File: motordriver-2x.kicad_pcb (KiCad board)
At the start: 4 copper layers, 641 parts, among them J1 USB_B_Micro, J2 CONN_RJ45_MAG, J3 CONN_RJ45_MAG, P1 CONN_BUTTON, P11 CONN_JOYSTICK, P13 CONN_SENSOR, P14 CONN_SENSOR, P15 CONN_SENSOR, P16 CONN_SENSOR, P17 CONN_DEBUG_2R, P18 CONN_POWER_41A, P19 CONN_CAN, P2 CONN_BUTTON, P20 CONN_CAN, P21 CONN_AN_OUT, P22 CONN_AN_OUT, P23 CONN_POWER_10A, P24 CONN_CAN, P25 CONN_LCD, P26 CONN_AN_OUT, P27 CONN_AN_OUT, P28 CONN_UEXT, P3 CONN_BUTTON, P37 ENCODER, P38 CONN_SENSOR, P39 CONN_SENSOR, P4 CONN_BUTTON, P40 CONN_SENSOR, P41 ENCODER, P42 CONN_SENSOR, P43 CONN_SENSOR, P44 CONN_SENSOR, P45 CONN_MOTOR, P46 CONN_MOTOR, P47 CONN_HALL, P48 CONN_HALL, P49 CONN_BRKRES, P5 CONN_BUTTON, P6 CONN_BUTTON, P7 CONN_BUTTON, P8 CONN_BUTTON, P9 CONN_JOYSTICK, Q1 Q_NMOS_2X_60V_63A, Q2 Q_NMOS_2X_60V_63A, Q3 Q_NMOS_2X_60V_63A, Q4 Q_NMOS_2X_60V_63A, Q5 Q_NMOS_2X_60V_63A, Q6 Q_NMOS_2X_60V_63A, Q7 Q_PNP_BC856, Q8 Q_NMOS_BUK9875, U1 IC_MIC2026, U10 IC_MCP4461, U11 IC_MCP2517FD-xJHA, U12 IC_STM32F429ZET6, U13 IC_MCP23S17, U14 IC_TPS54360DDA, U15 IC_TJA1044GT3, U16 IC_TLV2474, U17 IC_M24C16, U18 IC_USBLC6-2, U19 IC_TPS62147RGXR, U2 IC_MAX6818, U20 IC_TLV75533, U21 IC_LP55231, U22 IC_TLV75533, U23 IC_MAX14890, U24 IC_MAX14890, U25 IC_MIC2026, U26 IC_TLV2474, U27 IC_USBLC6-2, U28 IC_USBLC6-2, U29 IC_MCP4461, U3 IC_TLV2474, U30 IC_LAN9252, U31 IC_DRV8302, U32 IC_DRV8302, U33 IC_TLV2474, U34 IC_M24C16, U35 IC_TLV2474, U36 IC_TLV75533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

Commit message: power supply layout
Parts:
- added C51: CAP_2.2uF_16V_0402, Capacitor_SMD:C_0402_1005Metric, F.Cu at (377.4, -101.4)
- P37, P41: value ENCODER -> CONN_ENCODER
- moved U19 374.3 mm to (383.8, -120.2), turned to 90 degrees
- moved C55 359.3 mm to (389.0, -123.0), turned to 90 degrees
- moved C38 353.6 mm to (353.2, -114.0), turned to 180 degrees
- moved D16 351.6 mm to (387.0, -107.0), turned to 270 degrees
- moved C15 337.5 mm to (365.6, -120.2), turned to 90 degrees
- moved TP21 337.4 mm to (393.2, -117.4), turned to 90 degrees
- moved D9 335.2 mm to (350.6, -122.6), turned to 270 degrees
- moved R55 333.9 mm to (374.8, -112.0), turned to 90 degrees
- moved D28 333.7 mm to (356.6, -122.6), turned to 90 degrees
- moved D12 331.7 mm to (353.0, -107.0), turned to 180 degrees
- moved U22 331.1 mm to (380.4, -108.2)
- moved D30 326.1 mm to (387.0, -99.4), turned to 270 degrees
- moved R76 324.3 mm to (391.2, -101.6), turned to 180 degrees
- moved R58 317.3 mm to (387.4, -120.4)
- moved R62 316.7 mm to (377.4, -108.0)
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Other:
- board outline added: 200 x 127.2 mm
- board text added: "POWER"

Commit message: cpu layout
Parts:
- C28, C29, C34, C35, C39, C41, C42, C43, C44, C47, C48, C6: moved to B.Cu
- moved P20 228.2 mm to (323.0, 102.7), turned to 90 degrees
- moved U11 221.5 mm to (314.9, 107.3), turned to 90 degrees
- moved D10 214.8 mm to (318.0, 86.6)
- moved P19 211.7 mm to (323.0, 90.5), turned to 90 degrees
- moved D13 208.5 mm to (318.0, 100.6)
- moved P24 207.1 mm to (323.0, 114.8), turned to 90 degrees
- moved C42 200.6 mm to (38.2, 165.6)
- moved Y2 185.5 mm to (315.3, 112.9), turned to 270 degrees
- moved C43 184.7 mm to (48.6, 154.8), turned to 270 degrees
- moved C6 184.7 mm to (38.2, 171.2)
- moved C47 184.1 mm to (43.2, 154.8), turned to 270 degrees
- moved C44 176.5 mm to (38.2, 160.2)
- moved R198 176.0 mm to (51.4, 190.0)
- moved D31 175.0 mm to (54.0, 190.2)
- moved S1 168.6 mm to (66.4, 158.0)
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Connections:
- P19 pad 1: Net-(D10-Pad1) -> Net-(D10-Pad2)
- P19 pad 2: Net-(D10-Pad2) -> Net-(D10-Pad1)
- P20 pad 1: Net-(D11-Pad1) -> Net-(D11-Pad2)
- P20 pad 2: Net-(D11-Pad2) -> Net-(D11-Pad1)
- P24 pad 1: Net-(D13-Pad1) -> Net-(D13-Pad2)
- P24 pad 2: Net-(D13-Pad2) -> Net-(D13-Pad1)
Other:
- board text added: "CAN"

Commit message: save latest schematic
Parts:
- C111, C93: moved to F.Cu
- C40: moved to B.Cu
- moved R197 576.0 mm to (232.6, -414.4), turned to 270 degrees
- moved D29 574.1 mm to (223.2, -421.2)
- moved R196 572.5 mm to (241.6, -406.2), turned to 270 degrees
- moved TP61 570.8 mm to (165.2, -423.6)
- moved R43 570.0 mm to (209.0, -422.8), turned to 180 degrees
- moved Q7 569.5 mm to (239.2, -405.8)
- moved TP41 568.7 mm to (228.5, -405.2), turned to 180 degrees
- moved TP62 564.4 mm to (165.2, -424.6)
- moved Q8 563.6 mm to (237.8, -412.6)
- moved TP16 562.9 mm to (168.0, -446.1), turned to 180 degrees
- moved TP17 558.7 mm to (168.0, -445.2), turned to 180 degrees
- moved D27 554.3 mm to (235.0, -406.4)
- moved R195 551.8 mm to (233.0, -404.8), turned to 180 degrees
- moved TP55 540.1 mm to (228.5, -404.0), turned to 180 degrees
- moved TP81 532.7 mm to (12.1, -338.9)
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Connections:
- TP39 pad 1: Net-(R80-Pad2) -> Net-(R81-Pad2)
- TP40 pad 1: Net-(R82-Pad2) -> Net-(R83-Pad2)
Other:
- board size 200 x 127.2 mm -> 200 x 127.4 mm

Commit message: come up with pcb outline
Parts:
- added MT1: MOUNT_HOLE, MountingHole:MountingHole_3.2mm_M3_Pad, F.Cu at (255.7, 28.5)
- added MT2: MOUNT_HOLE, MountingHole:MountingHole_3.2mm_M3_Pad, F.Cu at (50.4, 148.7)
- added MT3: MOUNT_HOLE, MountingHole:MountingHole_3.2mm_M3_Pad, F.Cu at (255.0, 149.5)
- added MT4: MOUNT_HOLE, MountingHole:MountingHole_3.2mm_M3_Pad, F.Cu at (50.2, 29.0)
- C156, C157: moved to B.Cu
- moved R40 572.9 mm to (96.4, 100.9), turned to 0 degrees
- moved R49 572.3 mm to (104.0, 102.2), turned to 0 degrees
- moved R48 570.3 mm to (104.0, 101.2), turned to 180 degrees
- moved C166 568.4 mm to (104.0, 100.2), turned to 0 degrees
- moved C19 566.4 mm to (104.0, 99.2), turned to 0 degrees
- moved U14 565.2 mm to (99.0, 97.6), turned to 0 degrees
- moved R38 564.4 mm to (104.0, 98.2), turned to 0 degrees
- moved P23 563.0 mm to (113.2, 101.0), turned to 270 degrees
- moved C167 562.8 mm to (93.2, 92.7), turned to 0 degrees
- moved R37 562.5 mm to (104.0, 97.2), turned to 180 degrees
- moved D30 560.7 mm to (131.7, 101.9), turned to 270 degrees
- moved C18 560.5 mm to (104.0, 96.2), turned to 0 degrees
- moved R67 560.5 mm to (122.1, 100.9), turned to 0 degrees
- moved C165 560.1 mm to (93.2, 89.1), turned to 0 degrees
- moved U36 559.5 mm to (125.1, 100.7), turned to 0 degrees
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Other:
- board size 200 x 127.4 mm -> 215 x 130.1 mm
- board text removed: "MOTOR 2"
- board text removed: "POWER"
- board text removed: "Supply Sense"

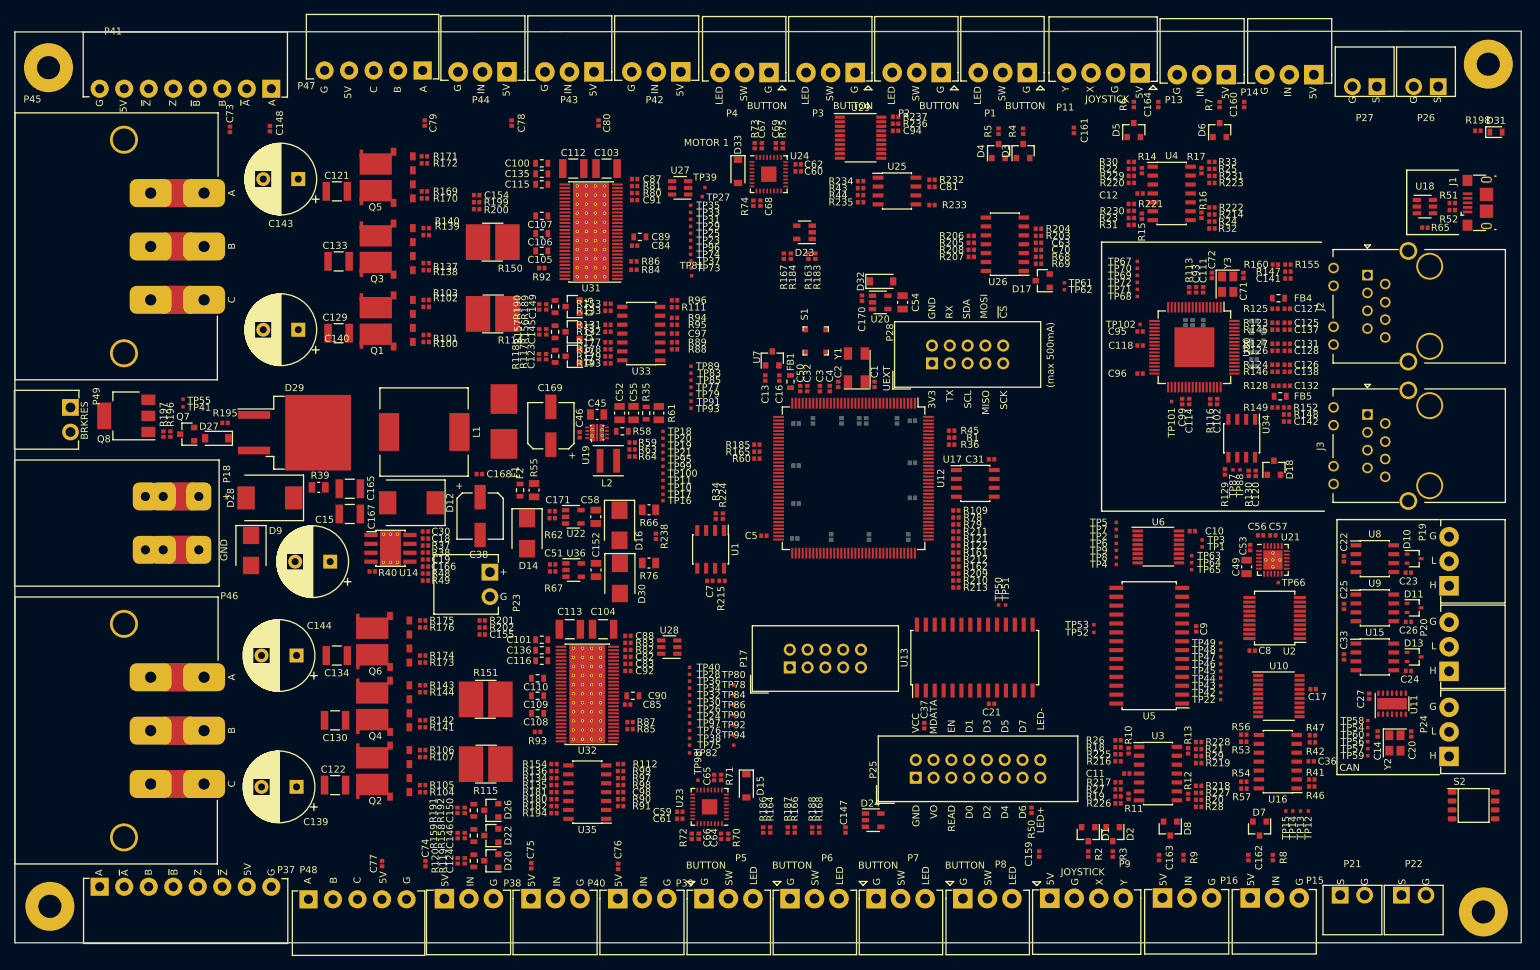
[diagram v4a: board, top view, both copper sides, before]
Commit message: better placement
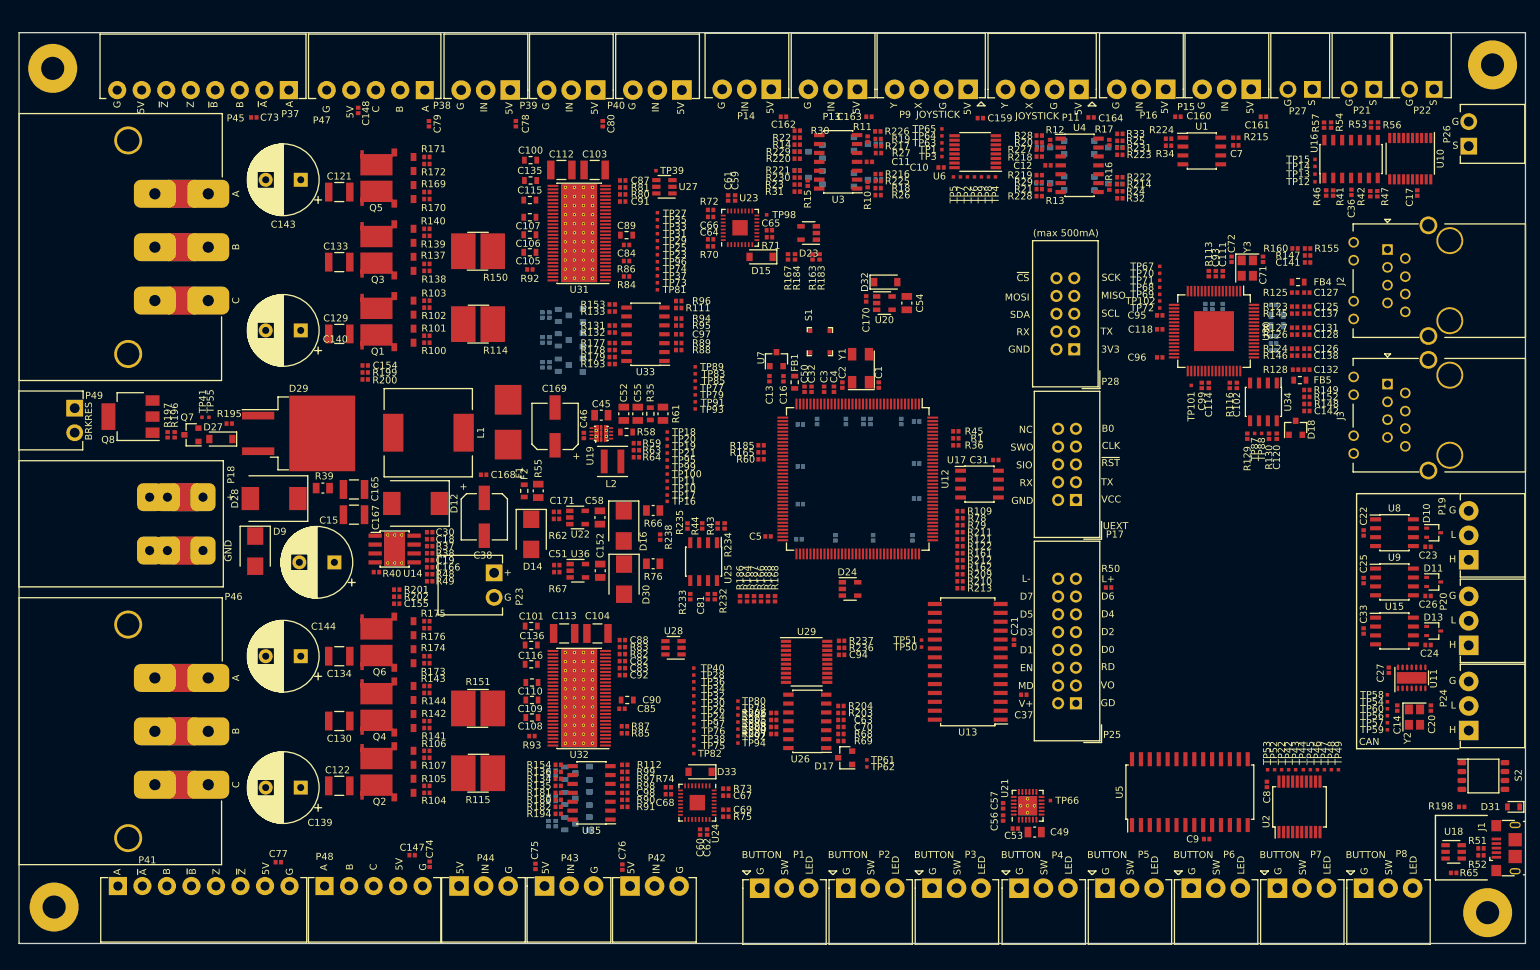
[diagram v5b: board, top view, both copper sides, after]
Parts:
- C123, C124, C145, C146, C149, C150, D1, D19, D2, D20, D21, D22, D25, D26, D3, D4, D5, D6, D7, D8, R117, R118, R119, R120, R156, R157, R158, R159, R189, R190, R191, R192, R2, R3, R4, R5, R6, R7, R8, R9: moved to B.Cu
- moved C162 124.8 mm to (155.1, 36.0), turned to 0 degrees
- moved P1 122.5 mm to (151.7, 146.1), turned to 0 degrees
- moved P4 121.7 mm to (188.7, 146.1), turned to 0 degrees
- moved P40 117.4 mm to (140.6, 32.2), turned to 180 degrees
- moved P2 117.2 mm to (164.0, 146.1), turned to 0 degrees
- moved P3 116.9 mm to (176.3, 146.1), turned to 0 degrees
- moved P37 116.9 mm to (84.5, 32.2), turned to 180 degrees
- moved P42 116.4 mm to (133.2, 145.8), turned to 0 degrees
- moved P43 116.4 mm to (121.0, 145.8), turned to 0 degrees
- moved P44 116.4 mm to (108.8, 145.8), turned to 0 degrees
- moved P9 116.0 mm to (181.5, 32.1), turned to 180 degrees
- moved P41 115.9 mm to (60.1, 145.8), turned to 0 degrees
- moved P38 115.8 mm to (116.1, 32.2), turned to 180 degrees
- moved P39 115.4 mm to (128.3, 32.2), turned to 180 degrees
- moved P16 115.4 mm to (209.7, 32.1), turned to 180 degrees
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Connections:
- U12 pad 69: ENCPWEN2 -> ENCPWEN1
- U12 pad 70: ENCPWEN1 -> ENCPWEN2
- U3 pad 10: Net-(D3-Pad3) -> Net-(D5-Pad3)
- U3 pad 12: Net-(D4-Pad3) -> Net-(D6-Pad3)
- U3 pad 13: Net-(R13-Pad2) -> Net-(R15-Pad2)
- U3 pad 14: Net-(R13-Pad1) -> Net-(R15-Pad1)
- U3 pad 8: Net-(R12-Pad1) -> Net-(R14-Pad1)
- U3 pad 9: Net-(R12-Pad2) -> Net-(R14-Pad2)
- U4 pad 1: Net-(R14-Pad1) -> Net-(R12-Pad1)
- U4 pad 2: Net-(R14-Pad2) -> Net-(R12-Pad2)
- U4 pad 3: Net-(D5-Pad3) -> Net-(D3-Pad3)
- U4 pad 5: Net-(D6-Pad3) -> Net-(D4-Pad3)
- U4 pad 6: Net-(R15-Pad2) -> Net-(R13-Pad2)
- U4 pad 7: Net-(R15-Pad1) -> Net-(R13-Pad1)
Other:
- board size 215 x 130.1 mm -> 215 x 130 mm
- board text removed: "MOTOR 1"

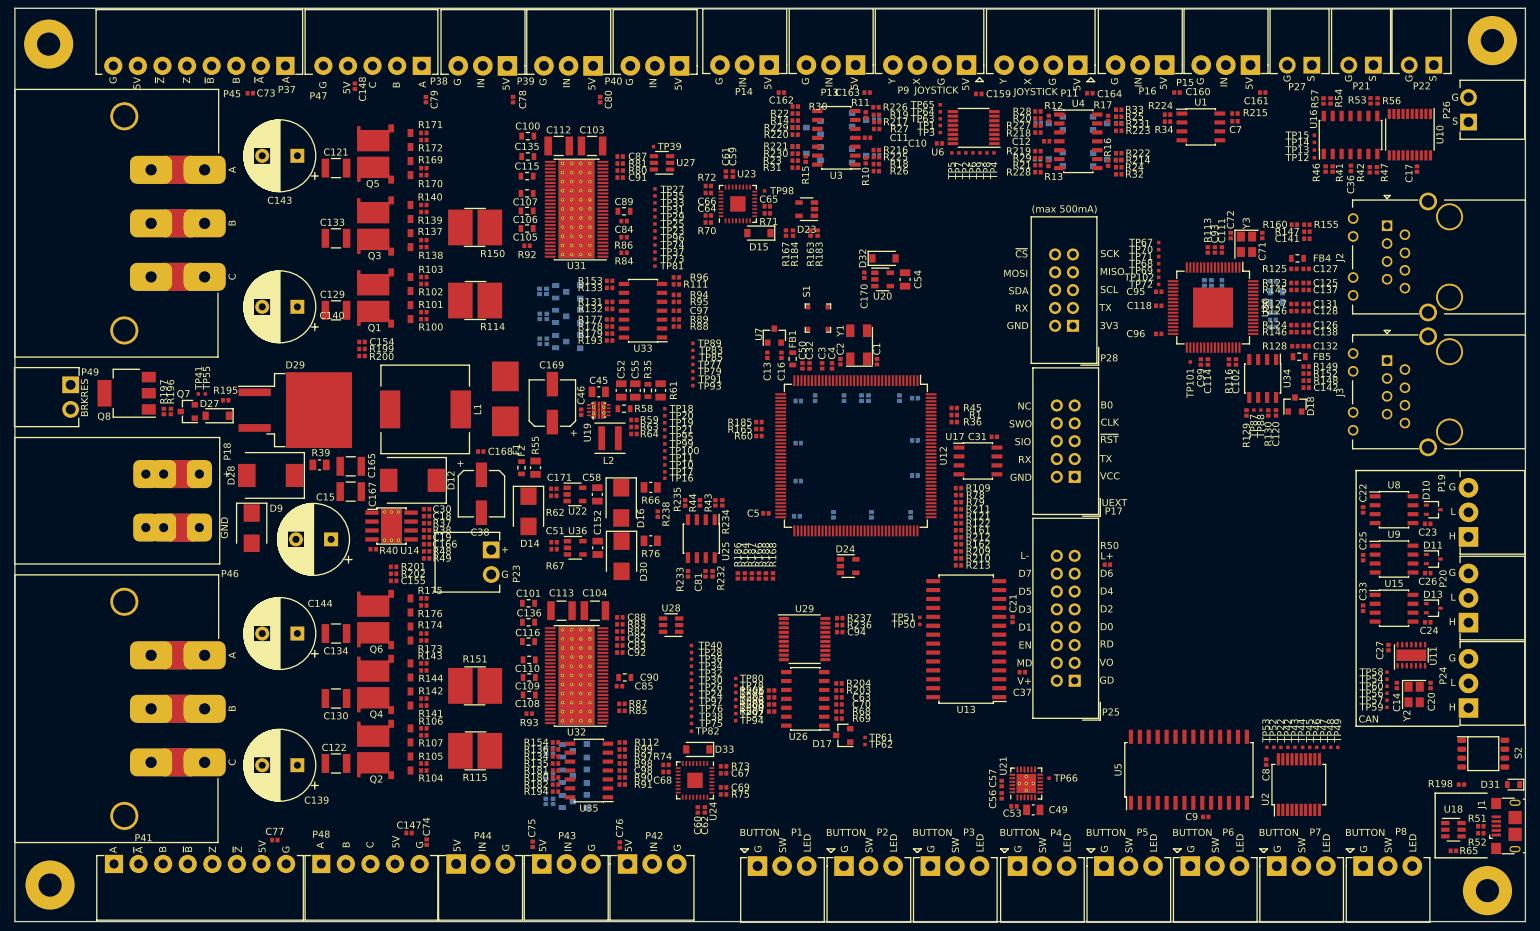
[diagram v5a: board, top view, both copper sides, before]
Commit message: create custom grounds
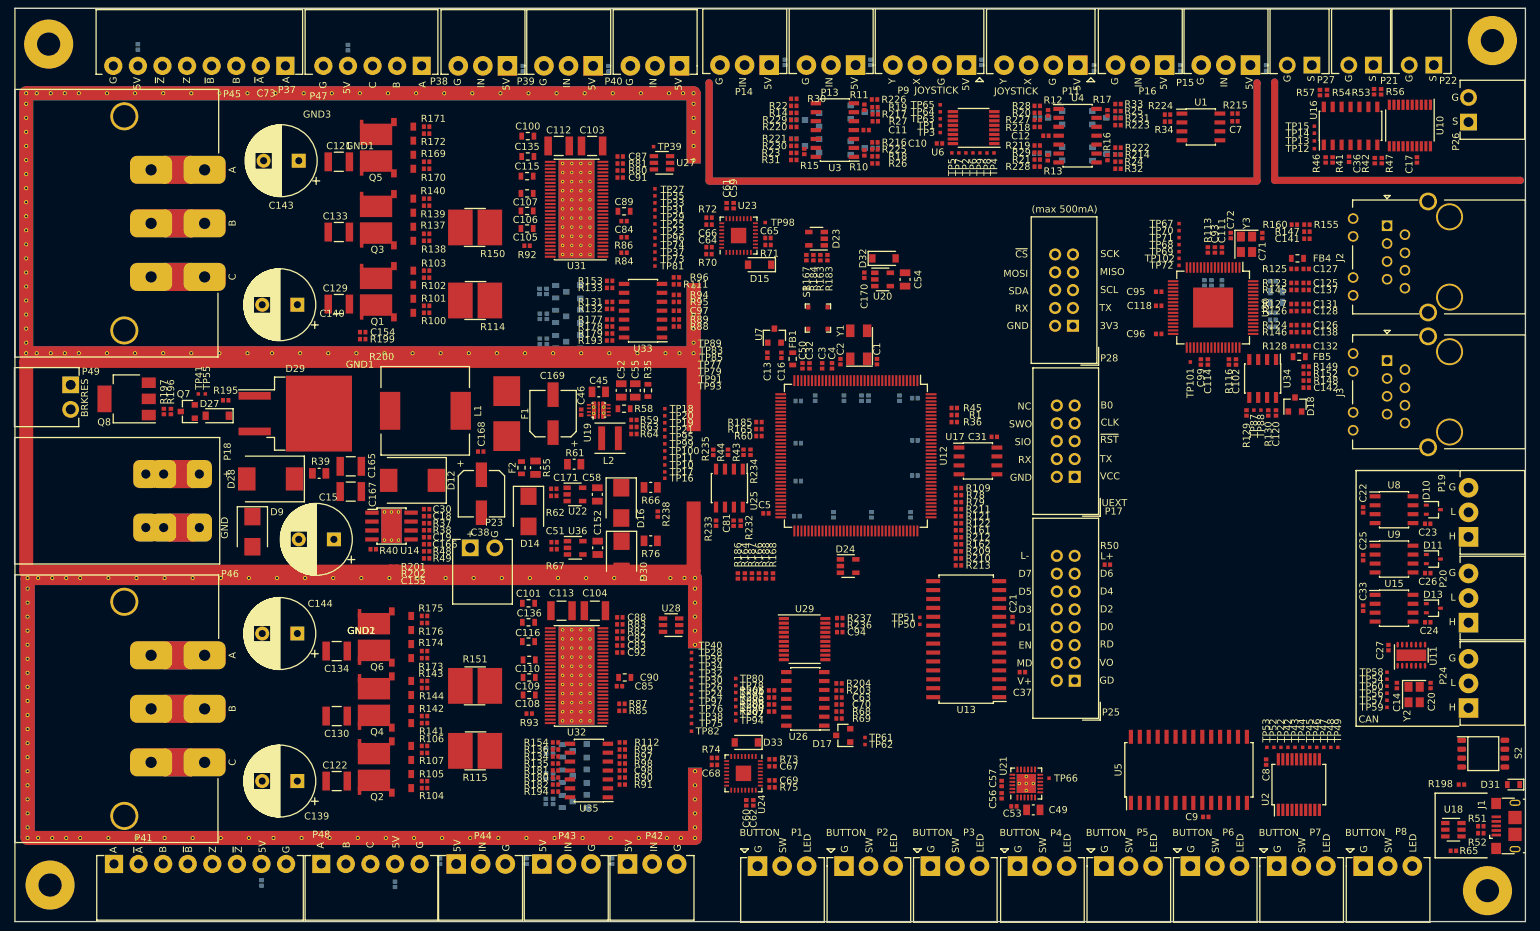
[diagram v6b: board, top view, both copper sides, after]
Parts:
- added GND1: GND_100X30, CUSTOM:GND_100X30, F.Cu at (95.1, 74.2)
- added GND2: GND_MOTOR_DRIVER, CUSTOM:GND_MOTOR_DRIVER, F.Cu at (95.3, 112.1)
- added GND3: GND_MOTOR_DRIVER, CUSTOM:GND_MOTOR_DRIVER, F.Cu at (95.1, 43.1)
- added GND4: GND_ANALOG_IN, CUSTOM:GND_ANALOG_IN, F.Cu at (183.8, 34.6)
- added GND5: GND_ANALOG_OUT, CUSTOM:GND_ANALOG_OUT, F.Cu at (242.8, 34.5)
- C147, C148, C159, C160, C161, C162, C163, C164, C74, C75, C76, C77, C78, C79, C80: moved to B.Cu
- moved C76 119.9 mm to (93.4, 29.6)
- moved C79 113.9 mm to (81.1, 148.5)
- moved C74 111.0 mm to (118.3, 32.6), turned to 90 degrees
- moved C75 110.9 mm to (130.5, 32.6), turned to 90 degrees
- moved C78 108.9 mm to (106.5, 145.4), turned to 270 degrees
- moved C80 108.4 mm to (131.0, 145.4), turned to 270 degrees
- moved C77 35.9 mm to (118.8, 145.4), turned to 270 degrees
- moved C148 31.4 mm to (63.5, 29.5), turned to 90 degrees
- moved R61 16.2 mm to (125.6, 88.9), turned to 0 degrees
- moved C81 8.24 mm to (148.3, 97.3), turned to 90 degrees
- moved R232 8.24 mm to (149.3, 97.3)
- moved R233 8.24 mm to (145.8, 97.3)
- moved R234 8.24 mm to (150.7, 87.2)
- moved R43 8.24 mm to (149.7, 87.2)
- moved R44 8.24 mm to (147.5, 87.2)
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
